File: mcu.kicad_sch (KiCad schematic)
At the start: 15 parts, among them SW1 RST, SW2 BOOT, U1 ESP32-S3-WROOM-1

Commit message: PCB schematic design
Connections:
- net USB_D-: now reaches U1.13 (USB_D-)
- net USB_D+: now reaches U1.14 (USB_D+)
- no-connect marks 0 -> 3
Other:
- moved on the sheet: D1, R1

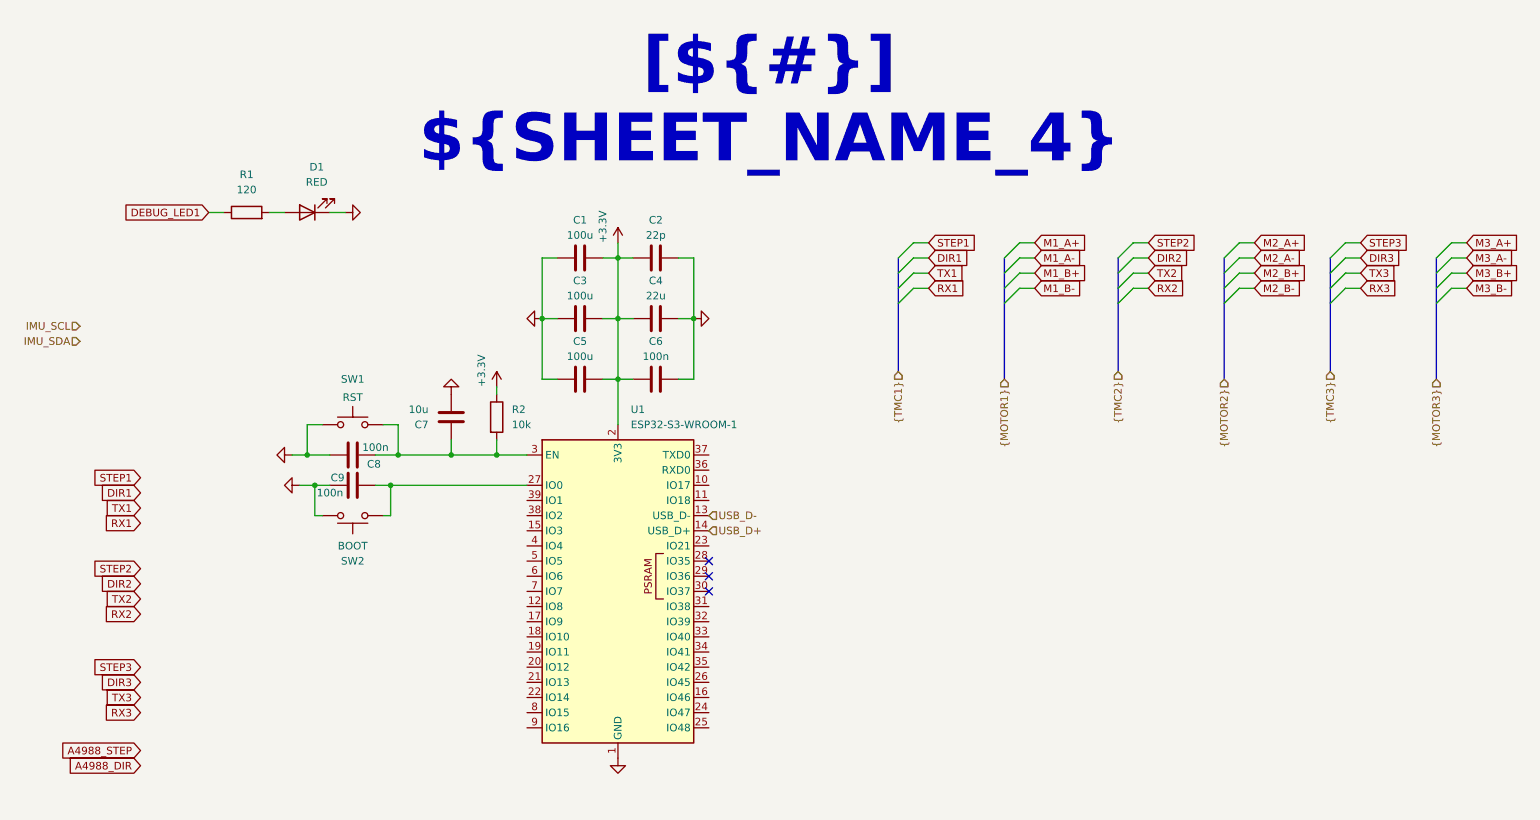
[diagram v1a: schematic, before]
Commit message: Connected hierarchical boards
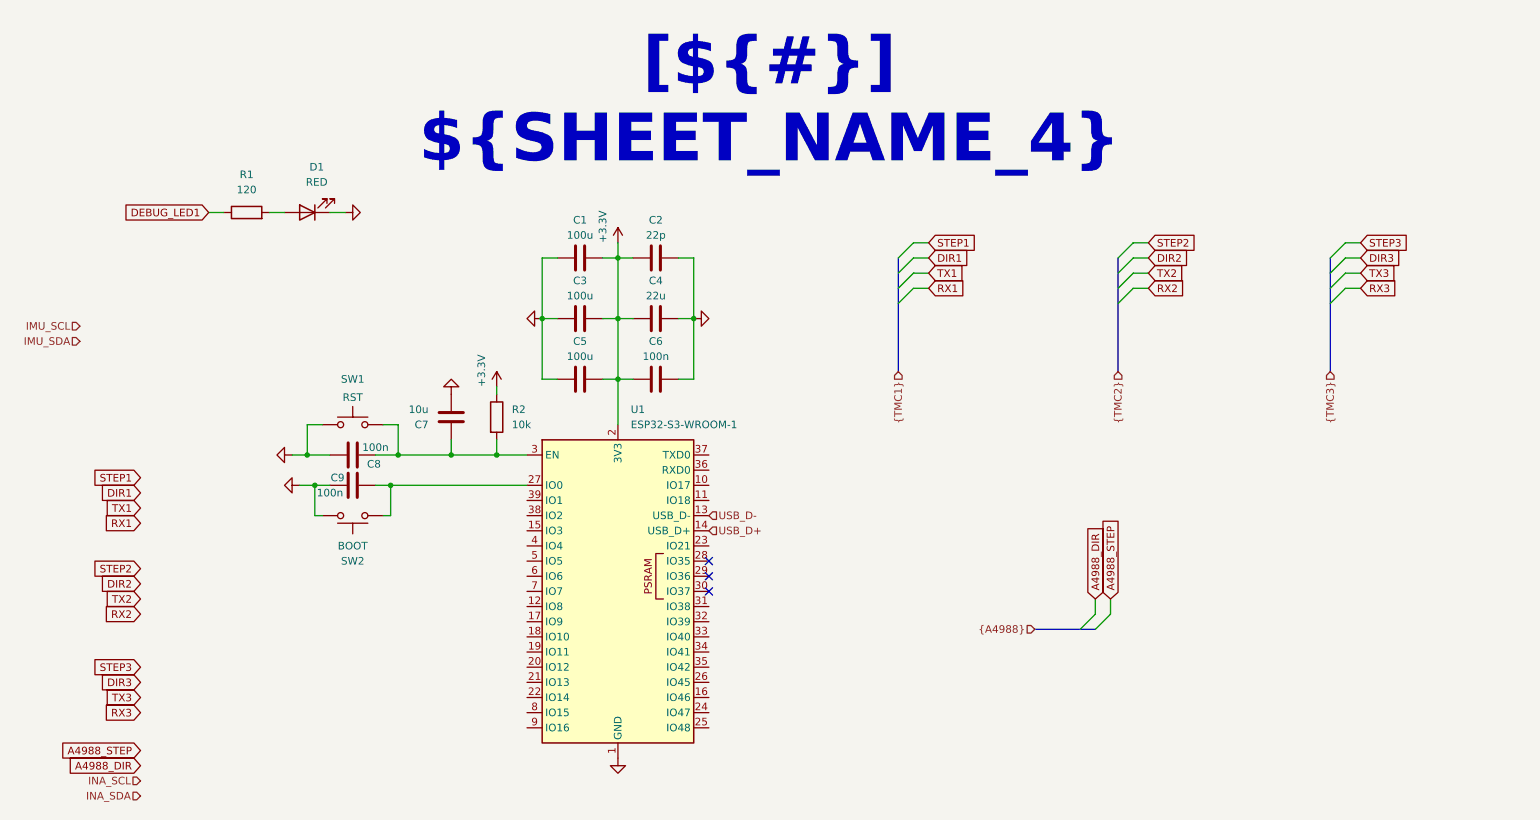
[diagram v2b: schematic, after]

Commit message: Finished design
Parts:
- added R34, R35, R36, R37: 47k, Resistor_SMD:R_0603_1608Metric_Pad0.98x0.95mm_HandSolder, symbol Device:R
- C1, C2, C3, C4, C5, C6, C7, C8, C9: footprint (none) -> Capacitor_SMD:C_0603_1608Metric_Pad1.08x0.95mm_HandSolder
- D1: footprint (none) -> LED_SMD:LED_0603_1608Metric_Pad1.05x0.95mm_HandSolder
- R1, R2: footprint (none) -> Resistor_SMD:R_0603_1608Metric_Pad0.98x0.95mm_HandSolder
- U1: footprint (none) -> Project_Components:ESP32-S3-WROOM-1_novias
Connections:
- net +3.3V: now also R34.1, R35.1, R36.1, R37.1
- net A4988_DIR: now also U1.19 (IO11)
- net A4988_STEP: now also U1.18 (IO10)
- net DEBUG_LED1: now also U1.39 (IO1)
- net DIR1: now also U1.7 (IO7)
- net DIR2: now also U1.10 (IO17)
- net DIR3: now also U1.16 (IO46)
- net IMU_SCL: now also U1.36 (RXD0), R34.2
- net IMU_SDA: now also U1.37 (TXD0), R35.2
- net INA_SCL: now also U1.21 (IO13), R37.2
- net INA_SDA: now also U1.20 (IO12), R36.2
- net RX1: now also U1.5 (IO5)
- net RX2: now also U1.9 (IO16)
- net RX3: now also U1.12 (IO8)
- net STEP1: now also U1.6 (IO6)
- net STEP2: now also U1.11 (IO18)
- net STEP3: now also U1.17 (IO9)
- net TX1: now also U1.4 (IO4)
- net TX2: now also U1.8 (IO15)
- net TX3: now also U1.15 (IO3)
- no-connect marks 3 -> 14
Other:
- note added: "DO NOT USE"

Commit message: Final tweaks
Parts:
- C1, C3, C5: footprint Capacitor_SMD:C_0603_1608Metric_Pad1.08x0.95mm_HandSolder -> Capacitor_SMD:C_1206_3216Metric_Pad1.33x1.80mm_HandSolder
- SW1, SW2: footprint Button_Switch_SMD:Panasonic_EVQPUJ_EVQPUA -> Button_Switch_SMD:SW_SPST_PTS647_Sx38
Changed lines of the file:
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@@
 			)
 		)
-		(property "Footprint" "Capacitor_SMD:C_0603_1608Metric_Pad1.08x0.95mm_HandSolder"
+		(property "Footprint" "Capacitor_SMD:C_1206_3216Metric_Pad1.33x1.80mm_HandSolder"
 			(at 118.11 53.6448 0)
 			(hide yes)
@@
 			)
 		)
-		(property "Footprint" "Button_Switch_SMD:Panasonic_EVQPUJ_EVQPUA"
+		(property "Footprint" "Button_Switch_SMD:SW_SPST_PTS647_Sx38"
 			(at 76.2 102.87 0)
 			(hide yes)
@@
 			)
 		)
-		(property "Footprint" "Capacitor_SMD:C_0603_1608Metric_Pad1.08x0.95mm_HandSolder"
+		(property "Footprint" "Capacitor_SMD:C_1206_3216Metric_Pad1.33x1.80mm_HandSolder"
 			(at 118.11 63.8048 0)
 			(hide yes)
@@
 			)
 		)
-		(property "Footprint" "Button_Switch_SMD:Panasonic_EVQPUJ_EVQPUA"
+		(property "Footprint" "Button_Switch_SMD:SW_SPST_PTS647_Sx38"
 			(at 76.2 77.47 0)
 			(hide yes)
@@
 			)
 		)
-		(property "Footprint" "Capacitor_SMD:C_0603_1608Metric_Pad1.08x0.95mm_HandSolder"
+		(property "Footprint" "Capacitor_SMD:C_1206_3216Metric_Pad1.33x1.80mm_HandSolder"
 			(at 118.11 73.9648 0)
 			(hide yes)

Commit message: Started troublefixing
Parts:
- renumbered R34 to R3, R35 to R4, R37 to R5, R36 to R6
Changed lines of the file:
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@@
 		(dnp no)
 		(fields_autoplaced yes)
-		(property "Reference" "#PWR08"
+		(property "Reference" "#PWR09"
 			(at 60.96 92.71 0)
 			(hide yes)
@@
 			(project "Orion"
 				(path "/f9e05184-c88b-4a88-ae9c-ab2bdb32be7c/c5103ceb-5325-4a84-a025-9638a412984e/582ab2b9-8009-4dea-9a22-6d88b1b0514a"
-					(reference "#PWR08")
+					(reference "#PWR09")
 					(unit 1)
 				)
@@
 		(dnp no)
 		(fields_autoplaced yes)
-		(property "Reference" "R37"
+		(property "Reference" "R5"
 			(at 74.93 132.0801 0)
 			(show_name no)
@@
 			(project "Orion"
 				(path "/f9e05184-c88b-4a88-ae9c-ab2bdb32be7c/c5103ceb-5325-4a84-a025-9638a412984e/582ab2b9-8009-4dea-9a22-6d88b1b0514a"
-					(reference "R37")
+					(reference "R5")
 					(unit 1)
 				)
@@
 		(dnp no)
 		(fields_autoplaced yes)
-		(property "Reference" "R34"
+		(property "Reference" "R3"
 			(at 152.4 80.0099 0)
 			(show_name no)
@@
 			(project "Orion"
 				(path "/f9e05184-c88b-4a88-ae9c-ab2bdb32be7c/c5103ceb-5325-4a84-a025-9638a412984e/582ab2b9-8009-4dea-9a22-6d88b1b0514a"
-					(reference "R34")
+					(reference "R3")
 					(unit 1)
 				)
@@
 		(in_pos_files yes)
 		(dnp no)
-		(property "Reference" "#PWR080"
+		(property "Reference" "#PWR011"
 			(at 86.36 135.89 0)
 			(hide yes)
@@
 			(project "Orion"
 				(path "/f9e05184-c88b-4a88-ae9c-ab2bdb32be7c/c5103ceb-5325-4a84-a025-9638a412984e/582ab2b9-8009-4dea-9a22-6d88b1b0514a"
-					(reference "#PWR080")
+					(reference "#PWR011")
 					(unit 1)
 				)
@@
 		(dnp no)
 		(fields_autoplaced yes)
-		(property "Reference" "#PWR07"
+		(property "Reference" "#PWR08"
 			(at 59.69 87.63 0)
 			(hide yes)
@@
 			(project "Orion"
 				(path "/f9e05184-c88b-4a88-ae9c-ab2bdb32be7c/c5103ceb-5325-4a84-a025-9638a412984e/582ab2b9-8009-4dea-9a22-6d88b1b0514a"
-					(reference "#PWR07")
+					(reference "#PWR08")
 					(unit 1)
 				)
@@
 		(in_pos_files yes)
 		(dnp no)
-		(property "Reference" "#PWR079"
+		(property "Reference" "#PWR05"
 			(at 149.86 76.2 0)
 			(hide yes)
@@
 			(project "Orion"
 				(path "/f9e05184-c88b-4a88-ae9c-ab2bdb32be7c/c5103ceb-5325-4a84-a025-9638a412984e/582ab2b9-8009-4dea-9a22-6d88b1b0514a"
-					(reference "#PWR079")
+					(reference "#PWR05")
 					(unit 1)
 				)
@@
 		(dnp no)
 		(fields_autoplaced yes)
-		(property "Reference" "R35"
+		(property "Reference" "R4"
 			(at 161.29 80.0099 0)
 			(show_name no)
@@
 			(project "Orion"
 				(path "/f9e05184-c88b-4a88-ae9c-ab2bdb32be7c/c5103ceb-5325-4a84-a025-9638a412984e/582ab2b9-8009-4dea-9a22-6d88b1b0514a"
-					(reference "R35")
+					(reference "R4")
 					(unit 1)
 				)
@@
 		(in_pos_files yes)
 		(dnp no)
-		(property "Reference" "#PWR05"
+		(property "Reference" "#PWR06"
 			(at 100.33 80.01 0)
 			(hide yes)
@@
 			(project "Orion"
 				(path "/f9e05184-c88b-4a88-ae9c-ab2bdb32be7c/c5103ceb-5325-4a84-a025-9638a412984e/582ab2b9-8009-4dea-9a22-6d88b1b0514a"
-					(reference "#PWR05")
+					(reference "#PWR06")
 					(unit 1)
 				)
@@
 		(dnp no)
 		(fields_autoplaced yes)
-		(property "Reference" "R36"
+		(property "Reference" "R6"
 			(at 83.82 132.0801 0)
 			(show_name no)
@@
 			(project "Orion"
 				(path "/f9e05184-c88b-4a88-ae9c-ab2bdb32be7c/c5103ceb-5325-4a84-a025-9638a412984e/582ab2b9-8009-4dea-9a22-6d88b1b0514a"
-					(reference "R36")
+					(reference "R6")
 					(unit 1)
 				)
@@
 		(dnp no)
 		(fields_autoplaced yes)
-		(property "Reference" "#PWR09"
+		(property "Reference" "#PWR010"
 			(at 120.65 144.78 0)
 			(hide yes)
@@
 			(project "Orion"
 				(path "/f9e05184-c88b-4a88-ae9c-ab2bdb32be7c/c5103ceb-5325-4a84-a025-9638a412984e/582ab2b9-8009-4dea-9a22-6d88b1b0514a"
-					(reference "#PWR09")
+					(reference "#PWR010")
 					(unit 1)
 				)
@@
 		(dnp no)
 		(fields_autoplaced yes)
-		(property "Reference" "#PWR06"
+		(property "Reference" "#PWR07"
 			(at 92.71 71.12 0)
 			(hide yes)
@@
 			(project "Orion"
 				(path "/f9e05184-c88b-4a88-ae9c-ab2bdb32be7c/c5103ceb-5325-4a84-a025-9638a412984e/582ab2b9-8009-4dea-9a22-6d88b1b0514a"
-					(reference "#PWR06")
-					(unit 1)
-				)
+					(reference "#PWR07")
+					(unit 1)
+				)

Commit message: Started rerouting changes
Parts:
- renumbered R3 to R34, R4 to R35, R6 to R36, R5 to R37
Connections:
- net DIR1: now also U1.6 (IO6); no longer U1.7 (IO7)
- net STEP1: now also U1.7 (IO7); no longer U1.6 (IO6)
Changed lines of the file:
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@@
 	(global_label "DIR1"
 		(shape input)
-		(at 105.41 110.49 180)
+		(at 105.41 107.95 180)
 		(fields_autoplaced yes)
 		(effects
@@
 		)
 		(property "Intersheetrefs" "${INTERSHEET_REFS}"
-			(at 98.0705 110.49 0)
+			(at 98.0705 107.95 0)
 			(hide yes)
 			(show_name no)
@@
 	(global_label "STEP1"
 		(shape input)
-		(at 105.41 107.95 180)
+		(at 105.41 110.49 180)
 		(fields_autoplaced yes)
 		(effects
@@
 		)
 		(property "Intersheetrefs" "${INTERSHEET_REFS}"
-			(at 96.6192 107.95 0)
+			(at 96.6192 110.49 0)
 			(hide yes)
 			(show_name no)
@@
 		(dnp no)
 		(fields_autoplaced yes)
-		(property "Reference" "R5"
+		(property "Reference" "R37"
 			(at 74.93 132.0801 0)
 			(show_name no)
@@
 			(project "Orion"
 				(path "/f9e05184-c88b-4a88-ae9c-ab2bdb32be7c/c5103ceb-5325-4a84-a025-9638a412984e/582ab2b9-8009-4dea-9a22-6d88b1b0514a"
-					(reference "R5")
+					(reference "R37")
 					(unit 1)
 				)
@@
 		(dnp no)
 		(fields_autoplaced yes)
-		(property "Reference" "R3"
+		(property "Reference" "R34"
 			(at 152.4 80.0099 0)
 			(show_name no)
@@
 			(project "Orion"
 				(path "/f9e05184-c88b-4a88-ae9c-ab2bdb32be7c/c5103ceb-5325-4a84-a025-9638a412984e/582ab2b9-8009-4dea-9a22-6d88b1b0514a"
-					(reference "R3")
+					(reference "R34")
 					(unit 1)
 				)
@@
 		(dnp no)
 		(fields_autoplaced yes)
-		(property "Reference" "R4"
+		(property "Reference" "R35"
 			(at 161.29 80.0099 0)
 			(show_name no)
@@
 			(project "Orion"
 				(path "/f9e05184-c88b-4a88-ae9c-ab2bdb32be7c/c5103ceb-5325-4a84-a025-9638a412984e/582ab2b9-8009-4dea-9a22-6d88b1b0514a"
-					(reference "R4")
+					(reference "R35")
 					(unit 1)
 				)
@@
 		(dnp no)
 		(fields_autoplaced yes)
-		(property "Reference" "R6"
+		(property "Reference" "R36"
 			(at 83.82 132.0801 0)
 			(show_name no)
@@
 			(project "Orion"
 				(path "/f9e05184-c88b-4a88-ae9c-ab2bdb32be7c/c5103ceb-5325-4a84-a025-9638a412984e/582ab2b9-8009-4dea-9a22-6d88b1b0514a"
-					(reference "R6")
+					(reference "R36")
 					(unit 1)
 				)
